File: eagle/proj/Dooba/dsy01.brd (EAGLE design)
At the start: 66.2 x 70.1 mm, 87 parts, among them P1 DIO, P10 SWD_CORE(SWCLK-SWDIO-GND), P11 SWD_CORE(SWCLK-SWDIO-GND), P2 CKI-CKO, P3 NOT, P4 RDY, P5 PWR(VIN-GND-RST), P6 SWD_CORE(SWCLK-SWDIO-GND), P7 SWD_CORE(SWCLK-SWDIO-GND), P8 SWD_CORE(SWCLK-SWDIO-GND), P9 SWD_CORE(SWCLK-SWDIO-GND), U1 STM32F071LQFP100, U10 S25FLXXXSSOIC16, U2 AS6C1608TSOPII-44, U3 STM32F030LQFP32, U5 STM32F030LQFP32, U6 STM32F030LQFP32, U7 STM32F030LQFP32, U8 MIC550XSOT23, U9 STM32F030LQFP32, X1 8MHz, X2 8MHz, X4 8MHz, X5 8MHz, X6 8MHz, X7 8MHz

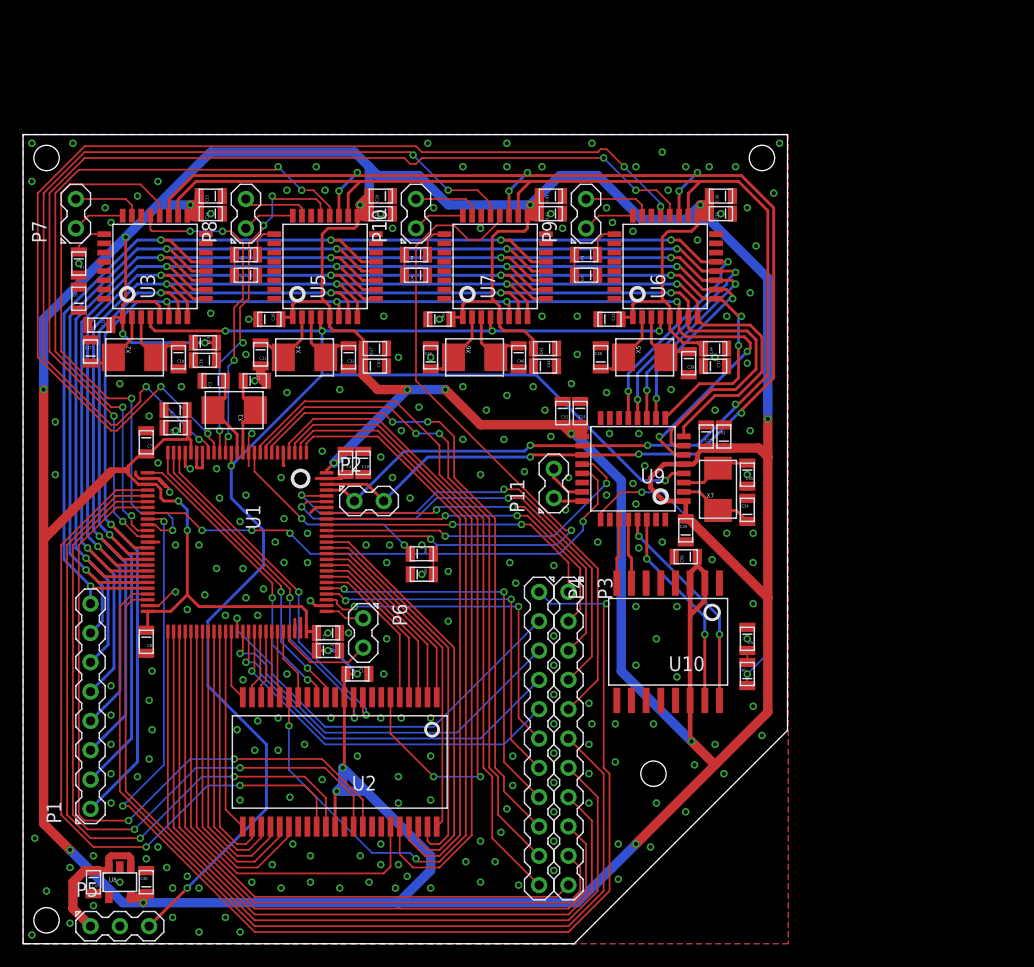
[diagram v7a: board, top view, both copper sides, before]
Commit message: Started decorating DSY01
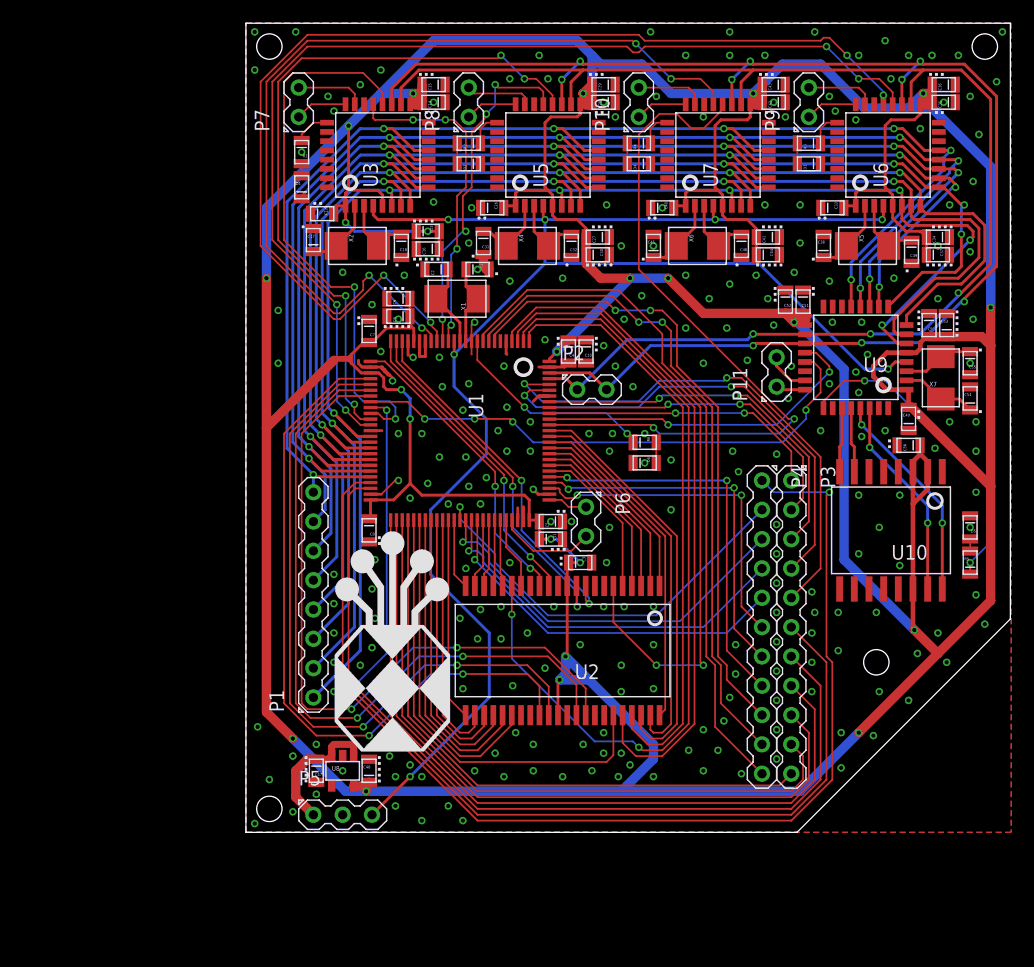
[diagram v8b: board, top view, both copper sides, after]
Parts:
- moved C38 21.6 mm to (81.5, 66.8)
- moved C45 21.6 mm to (66.8, 66.8)
- moved C30 21.6 mm to (62.0, 66.0)
- moved C33 21.6 mm to (82.3, 70.1)
- moved C37 21.6 mm to (91.4, 66.0)
- moved D1 21.6 mm to (36.3, 71.9)
- moved D6 21.6 mm to (66.0, 48.0)
- moved R6 21.6 mm to (66.0, 49.8)
- moved X2 21.6 mm to (41.1, 66.8)
- moved X4 21.6 mm to (55.9, 66.8)
- moved C10 21.6 mm to (61.0, 57.7)
- moved C11 21.6 mm to (57.9, 41.4)
- moved C12 21.6 mm to (38.1, 69.6)
- moved C14 21.6 mm to (47.8, 79.2)
- moved C15 21.6 mm to (47.8, 80.8)
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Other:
- board text added: "-------------> 27pF"
- board text added: "----------> 100nF"
- board text added: "-------> 4.7uF"
- board text added: "----> 10nF"
- board text added: "-> 1uF"
- board text added: "Dooba DSY01 by Eresse <eresse@eresse.net>"
